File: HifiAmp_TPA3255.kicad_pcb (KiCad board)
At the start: 4 copper layers, 200 x 150 mm, 124 parts, among them J1 PVDD 48V IN — NEEDS_DATA, J2 RCA L SE, J3 RCA R SE, J301 SPK_L, J302 SPK_R, J4 VOLUME_REMOTE, Q301 IPP330P10NM, Q302 IXTK200N10L2, U1 LM5010ASD, U2 LM2940IMP-12/NOPB, U3 TLV1117-33IDCY, U4 OPA1612AIDR, U5 OPA1612AIDR, U6 TPA3255B, U7 TPS3802K33DCKR, U8 LM5069-2

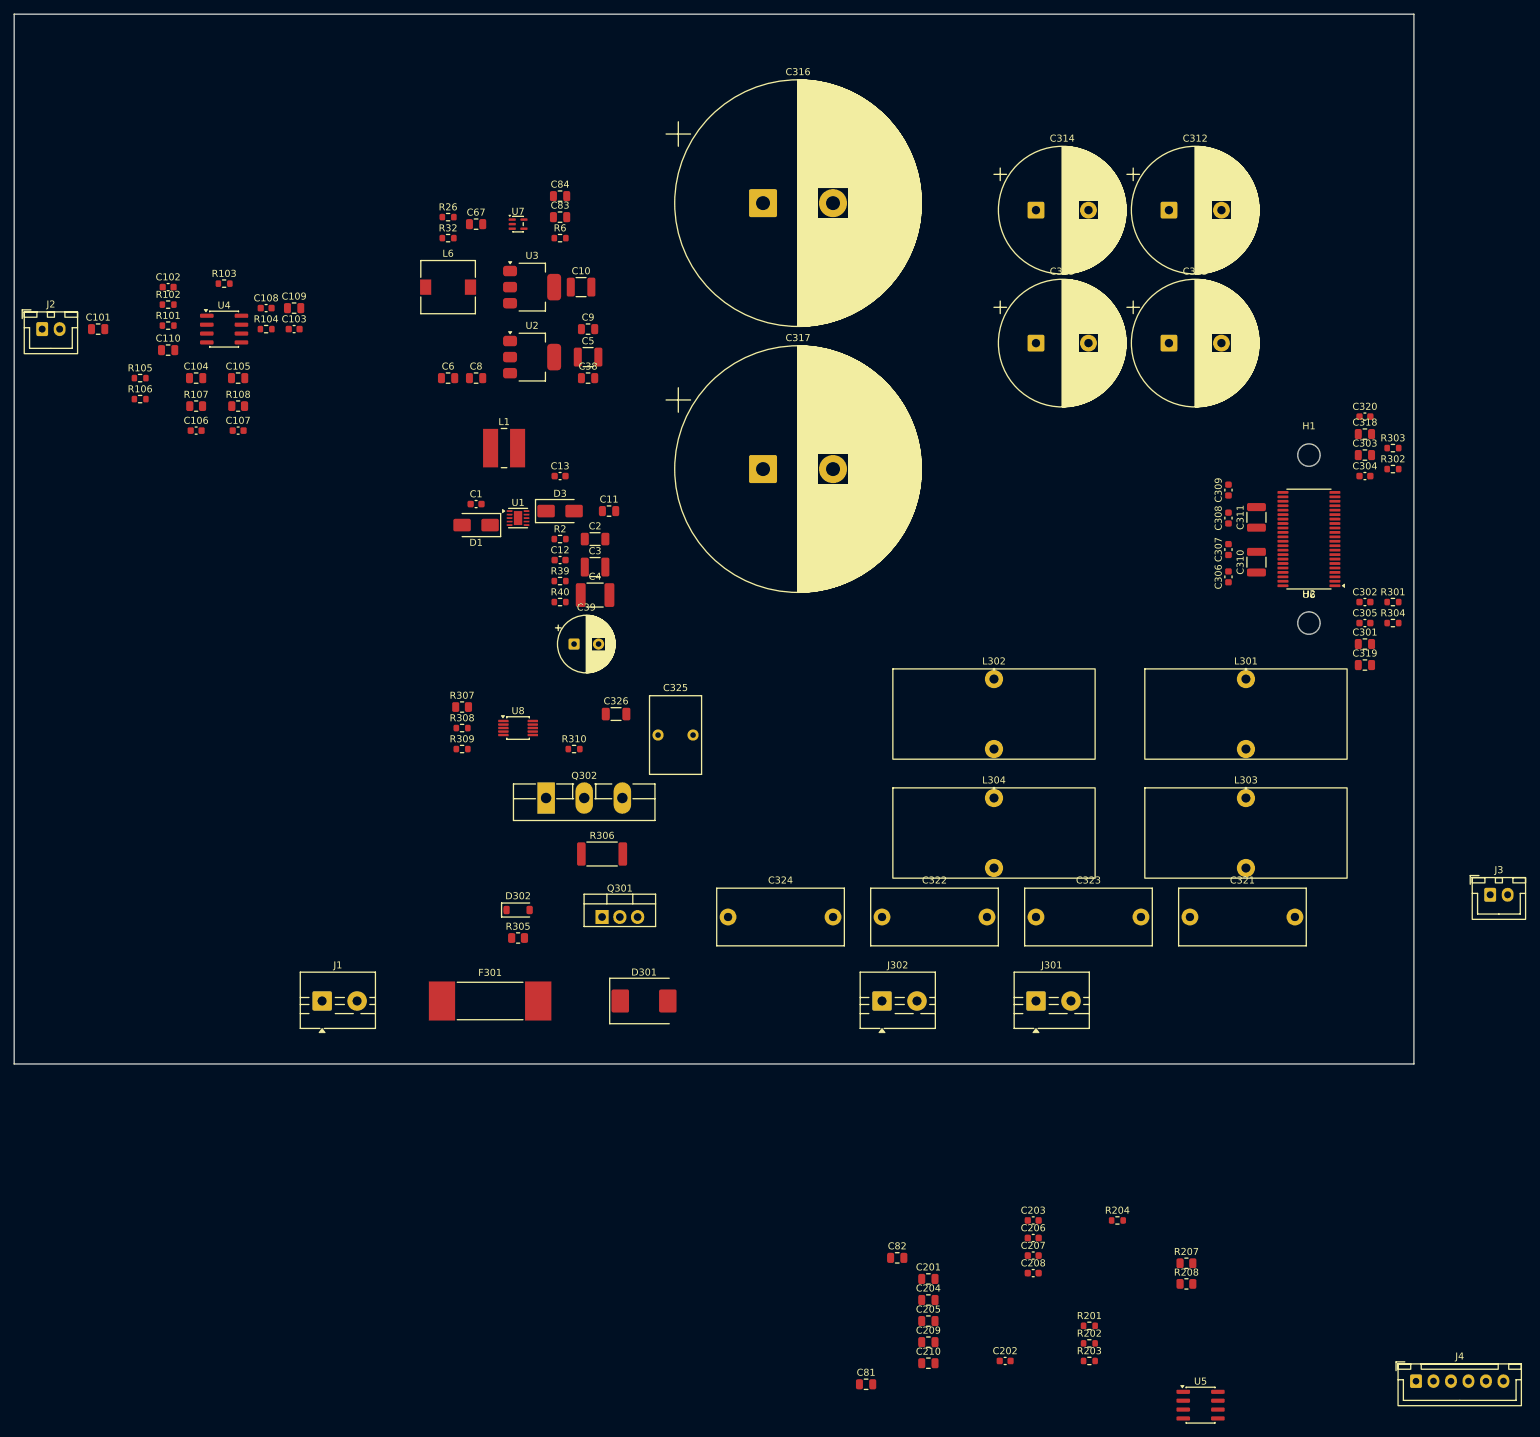
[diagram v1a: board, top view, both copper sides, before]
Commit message: feat(e1.4): mirror the left channel onto the right, and close the placement
The last 21 footprints go down as a pure translation of the left channel,
+40 mm in y and same x: U5 at (130, 185) against U4 at (130, 145), each
series-200 satellite on its series-100 twin's homologue. C210 stays glued to
U5 for the reason C110 stays glued to U4. C81/C82 close the +12V-OA rail
downstream of L6, and J3/J4 leave through the front panel. Nothing crosses
x = 156, where E1.3's auxiliary supply block starts.

The translation is deliberate rather than convenient: it lets E1.5 judge
inter-channel symmetry on measured geometry instead of on stated intent.

The import block is now empty — all 124 footprints are placed.

DRC: 104 violations, all silkscreen (85 silk_overlap, 19 silk_over_copper);
no clearance, no courtyards_overlap, lib_footprint_mismatch still 0;
pad_prop_heatsink still present once, so E1.10's regression did not recur;
schematic_parity 0; 254 unconnected. The diff touches 21 (at ...) lines and
nothing else, which is what proves the 103 earlier placements intact.

Co-Authored-By: Claude Opus 5 <noreply@anthropic.com>
Claude-Session: https://claude.ai/code/session_01JQiSdGemgJKtPWgNcZMmbY
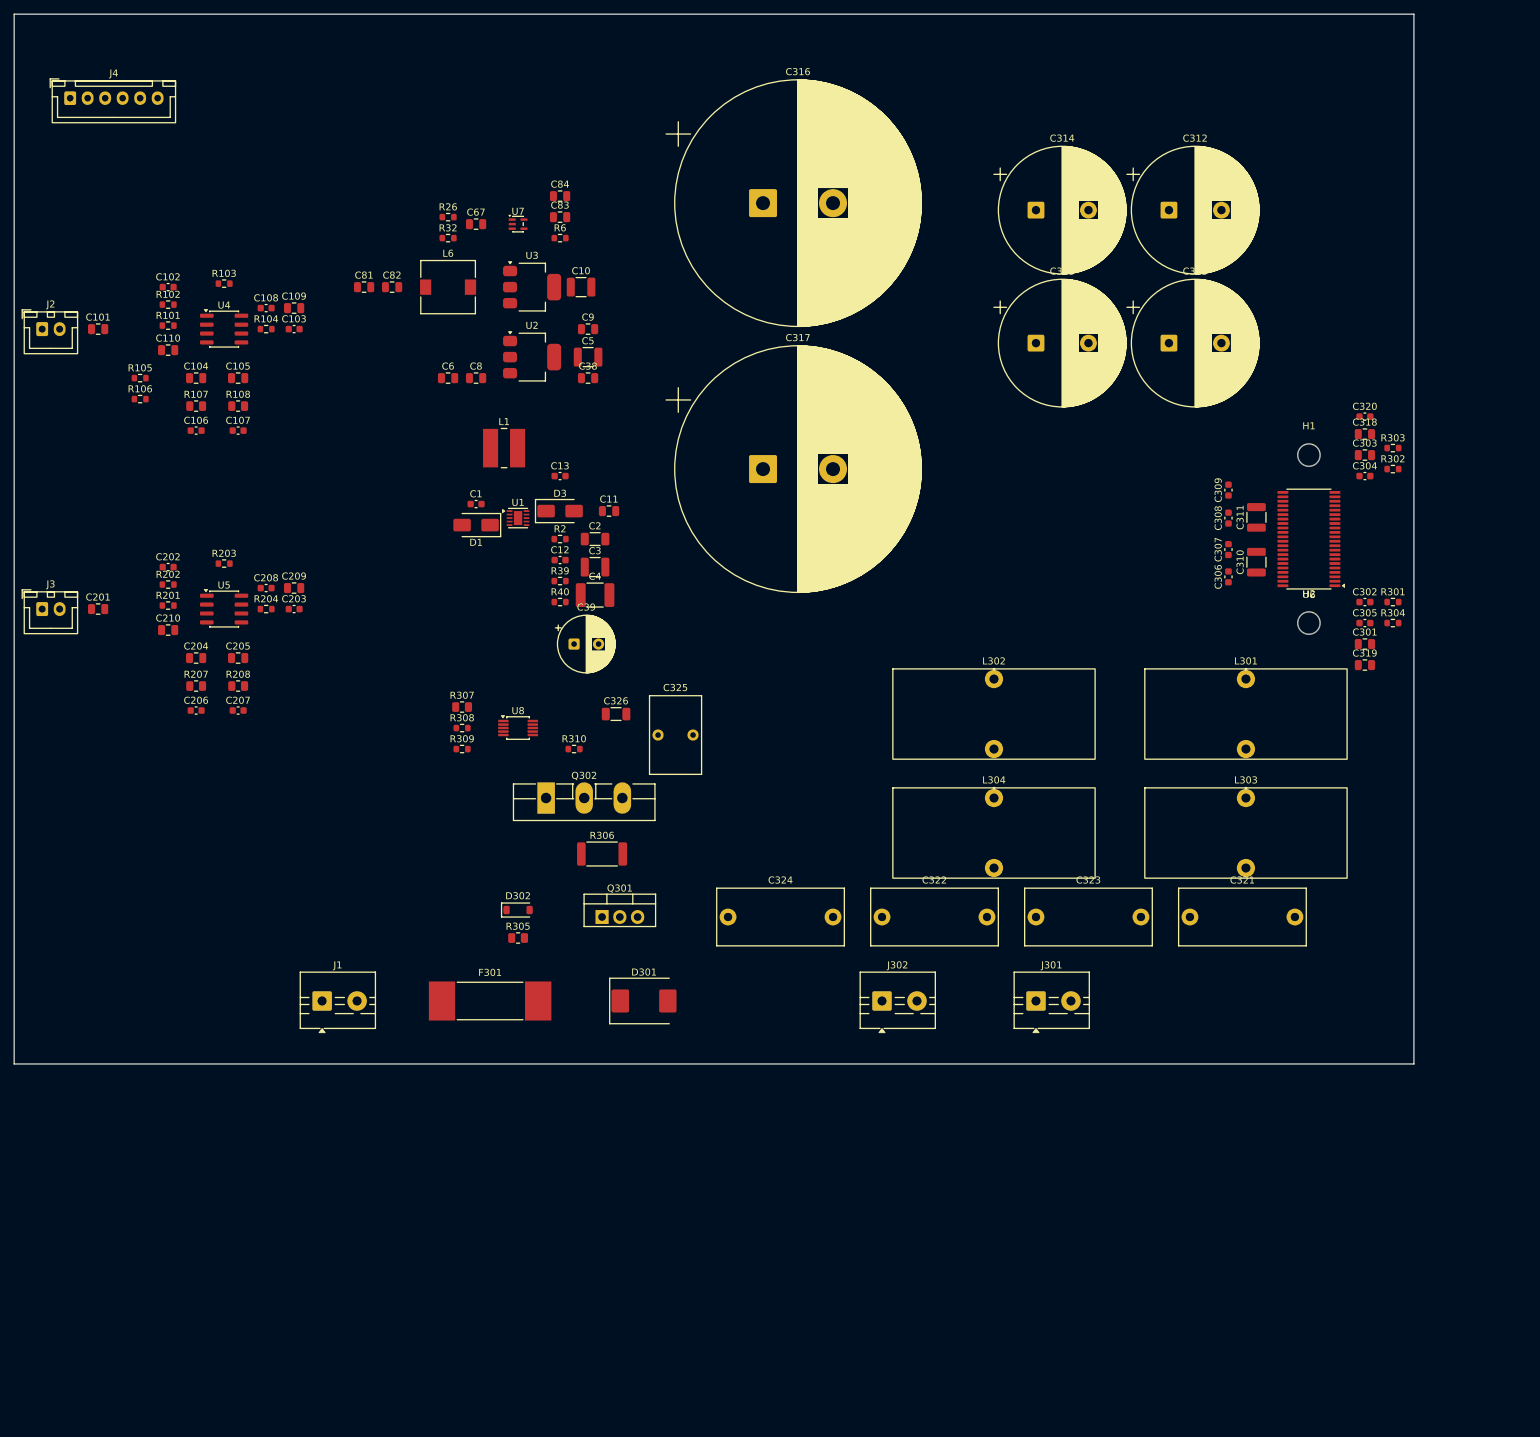
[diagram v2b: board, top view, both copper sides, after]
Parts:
- moved J4 265.7 mm to (108.0, 112.0)
- moved J3 210.9 mm to (104.0, 185.0)
- moved U5 180.0 mm to (130.0, 185.0)
- moved C81 172.4 mm to (150.0, 139.0)
- moved R202 170.5 mm to (122.0, 181.5)
- moved R203 168.1 mm to (130.0, 178.5)
- moved R201 167.1 mm to (122.0, 184.5)
- moved C202 164.8 mm to (122.0, 179.0)
- moved R207 163.8 mm to (126.0, 196.0)
- moved R208 160.2 mm to (132.0, 196.0)
- moved C82 156.4 mm to (154.0, 139.0)
- moved C201 152.4 mm to (112.0, 185.0)
- moved C210 150.9 mm to (122.0, 188.0)
- moved R204 149.8 mm to (136.0, 185.0)
- moved C208 147.0 mm to (136.0, 182.0)
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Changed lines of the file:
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@@
 	(footprint "Resistor_SMD:R_0603_1608Metric"
 		(layer "F.Cu")
-		(at 257.635 272.355)
+		(at 136 185)
 		(descr "Resistor SMD 0603 (1608 Metric), square (rectangular) end terminal, IPC-7351 nominal, (Body size source: IPC-SM-782 page 72, https://www.pcb-3d.com/wordpress/wp-content/uploads/ipc-sm-782a_amendment_1_and_2.pdf)")
 		(tags "resistor")
@@
 	(footprint "Connector_JST:JST_XH_B2B-XH-A_1x02_P2.50mm_Vertical"
 		(layer "F.Cu")
-		(at 310.895 225.825)
+		(at 104 185)
 		(descr "JST XH series connector, B2B-XH-A (http://www.jst-mfg.com/product/pdf/eng/eXH.pdf)")
 		(tags "connector JST XH vertical")
@@
 	(footprint "Capacitor_SMD:C_0805_2012Metric"
 		(layer "F.Cu")
-		(at 230.625 283.725)
+		(at 126 192)
 		(descr "Capacitor SMD 0805 (2012 Metric), square (rectangular) end terminal, IPC-7351 nominal, (Body size source: IPC-SM-782 page 76, https://www.pcb-3d.com/wordpress/wp-content/uploads/ipc-sm-782a_amendment_1_and_2.pdf, https://docs.google.com/spreadsheets/d/1BsfQQcO9C6DZCsRaXUlFlo91Tg2WpOkGARC1WS5S8t0/edit?usp=sharing)")
 		(tags "capacitor")
@@
 	(footprint "Capacitor_SMD:C_0603_1608Metric"
 		(layer "F.Cu")
-		(at 241.595 292.435)
+		(at 122 179)
 		(descr "Capacitor SMD 0603 (1608 Metric), square (rectangular) end terminal, IPC-7351 nominal, (Body size source: IPC-SM-782 page 76, https://www.pcb-3d.com/wordpress/wp-content/uploads/ipc-sm-782a_amendment_1_and_2.pdf)")
 		(tags "capacitor")
@@
 	(footprint "Capacitor_SMD:C_0603_1608Metric"
 		(layer "F.Cu")
-		(at 245.605 274.865)
+		(at 126 199.5)
 		(descr "Capacitor SMD 0603 (1608 Metric), square (rectangular) end terminal, IPC-7351 nominal, (Body size source: IPC-SM-782 page 76, https://www.pcb-3d.com/wordpress/wp-content/uploads/ipc-sm-782a_amendment_1_and_2.pdf)")
 		(tags "capacitor")
@@
 	(footprint "Capacitor_SMD:C_0805_2012Metric"
 		(layer "F.Cu")
-		(at 230.625 289.745)
+		(at 140 182)
 		(descr "Capacitor SMD 0805 (2012 Metric), square (rectangular) end terminal, IPC-7351 nominal, (Body size source: IPC-SM-782 page 76, https://www.pcb-3d.com/wordpress/wp-content/uploads/ipc-sm-782a_amendment_1_and_2.pdf, https://docs.google.com/spreadsheets/d/1BsfQQcO9C6DZCsRaXUlFlo91Tg2WpOkGARC1WS5S8t0/edit?usp=sharing)")
 		(tags "capacitor")
@@
 	(footprint "Capacitor_SMD:C_0603_1608Metric"
 		(layer "F.Cu")
-		(at 245.605 277.375)
+		(at 132 199.5)
 		(descr "Capacitor SMD 0603 (1608 Metric), square (rectangular) end terminal, IPC-7351 nominal, (Body size source: IPC-SM-782 page 76, https://www.pcb-3d.com/wordpress/wp-content/uploads/ipc-sm-782a_amendment_1_and_2.pdf)")
 		(tags "capacitor")
@@
 	(footprint "Package_SO:SOIC-8_3.9x4.9mm_P1.27mm"
 		(layer "F.Cu")
-		(at 269.515 298.745)
+		(at 130 185)
 		(descr "SOIC, 8 Pin (JEDEC MS-012AA, https://www.analog.com/media/en/package-pcb-resources/package/pkg_pdf/soic_narrow-r/r_8.pdf)")
 		(tags "SOIC SO")
@@
 	(footprint "Capacitor_SMD:C_0603_1608Metric"
 		(layer "F.Cu")
-		(at 245.605 272.355)
+		(at 140 185)
 		(descr "Capacitor SMD 0603 (1608 Metric), square (rectangular) end terminal, IPC-7351 nominal, (Body size source: IPC-SM-782 page 76, https://www.pcb-3d.com/wordpress/wp-content/uploads/ipc-sm-782a_amendment_1_and_2.pdf)")
 		(tags "capacitor")
@@
 	(footprint "Resistor_SMD:R_0603_1608Metric"
 		(layer "F.Cu")
-		(at 253.625 289.925)
+		(at 122 181.5)
 		(descr "Resistor SMD 0603 (1608 Metric), square (rectangular) end terminal, IPC-7351 nominal, (Body size source: IPC-SM-782 page 72, https://www.pcb-3d.com/wordpress/wp-content/uploads/ipc-sm-782a_amendment_1_and_2.pdf)")
 		(tags "resistor")
@@
 	(footprint "Capacitor_SMD:C_0805_2012Metric"
 		(layer "F.Cu")
-		(at 230.625 286.735)
+		(at 132 192)
 		(descr "Capacitor SMD 0805 (2012 Metric), square (rectangular) end terminal, IPC-7351 nominal, (Body size source: IPC-SM-782 page 76, https://www.pcb-3d.com/wordpress/wp-content/uploads/ipc-sm-782a_amendment_1_and_2.pdf, https://docs.google.com/spreadsheets/d/1BsfQQcO9C6DZCsRaXUlFlo91Tg2WpOkGARC1WS5S8t0/edit?usp=sharing)")
 		(tags "capacitor")
@@
 	(footprint "Connector_JST:JST_XH_B6B-XH-A_1x06_P2.50mm_Vertical"
 		(layer "F.Cu")
-		(at 300.295 295.315)
+		(at 108 112)
 		(descr "JST XH series connector, B6B-XH-A (http://www.jst-mfg.com/product/pdf/eng/eXH.pdf)")
 		(tags "connector JST XH vertical")
@@
 	(footprint "Resistor_SMD:R_0805_2012Metric"
 		(layer "F.Cu")
-		(at 267.495 278.475)
+		(at 126 196)
 		(descr "Resistor SMD 0805 (2012 Metric), square (rectangular) end terminal, IPC-7351 nominal, (Body size source: IPC-SM-782 page 72, https://www.pcb-3d.com/wordpress/wp-content/uploads/ipc-sm-782a_amendment_1_and_2.pdf)")
 		(tags "resistor")
@@
 	(footprint "Resistor_SMD:R_0603_1608Metric"
 		(layer "F.Cu")
-		(at 253.625 287.415)
+		(at 122 184.5)
 		(descr "Resistor SMD 0603 (1608 Metric), square (rectangular) end terminal, IPC-7351 nominal, (Body size source: IPC-SM-782 page 72, https://www.pcb-3d.com/wordpress/wp-content/uploads/ipc-sm-782a_amendment_1_and_2.pdf)")
 		(tags "resistor")
@@
 	(footprint "Capacitor_SMD:C_0805_2012Metric"
 		(layer "F.Cu")
-		(at 221.725 295.765)
+		(at 150 139)
 		(descr "Capacitor SMD 0805 (2012 Metric), square (rectangular) end terminal, IPC-7351 nominal, (Body size source: IPC-SM-782 page 76, https://www.pcb-3d.com/wordpress/wp-content/uploads/ipc-sm-782a_amendment_1_and_2.pdf, https://docs.google.com/spreadsheets/d/1BsfQQcO9C6DZCsRaXUlFlo91Tg2WpOkGARC1WS5S8t0/edit?usp=sharing)")
 		(tags "capacitor")
@@
 	(footprint "Capacitor_SMD:C_0805_2012Metric"
 		(layer "F.Cu")
-		(at 230.625 292.755)
+		(at 122 188)
 		(descr "Capacitor SMD 0805 (2012 Metric), square (rectangular) end terminal, IPC-7351 nominal, (Body size source: IPC-SM-782 page 76, https://www.pcb-3d.com/wordpress/wp-content/uploads/ipc-sm-782a_amendment_1_and_2.pdf, https://docs.google.com/spreadsheets/d/1BsfQQcO9C6DZCsRaXUlFlo91Tg2WpOkGARC1WS5S8t0/edit?usp=sharing)")
 		(tags "capacitor")
@@
 	(footprint "Capacitor_SMD:C_0805_2012Metric"
 		(layer "F.Cu")
-		(at 230.625 280.715)
+		(at 112 185)
 		(descr "Capacitor SMD 0805 (2012 Metric), square (rectangular) end terminal, IPC-7351 nominal, (Body size source: IPC-SM-782 page 76, https://www.pcb-3d.com/wordpress/wp-content/uploads/ipc-sm-782a_amendment_1_and_2.pdf, https://docs.google.com/spreadsheets/d/1BsfQQcO9C6DZCsRaXUlFlo91Tg2WpOkGARC1WS5S8t0/edit?usp=sharing)")
 		(tags "capacitor")
@@
 	(footprint "Capacitor_SMD:C_0805_2012Metric"
 		(layer "F.Cu")
-		(at 226.175 277.705)
+		(at 154 139)
 		(descr "Capacitor SMD 0805 (2012 Metric), square (rectangular) end terminal, IPC-7351 nominal, (Body size source: IPC-SM-782 page 76, https://www.pcb-3d.com/wordpress/wp-content/uploads/ipc-sm-782a_amendment_1_and_2.pdf, https://docs.google.com/spreadsheets/d/1BsfQQcO9C6DZCsRaXUlFlo91Tg2WpOkGARC1WS5S8t0/edit?usp=sharing)")
 		(tags "capacitor")
@@
 	(footprint "Capacitor_SMD:C_0603_1608Metric"
 		(layer "F.Cu")
-		(at 245.605 279.885)
+		(at 136 182)
 		(descr "Capacitor SMD 0603 (1608 Metric), square (rectangular) end terminal, IPC-7351 nominal, (Body size source: IPC-SM-782 page 76, https://www.pcb-3d.com/wordpress/wp-content/uploads/ipc-sm-782a_amendment_1_and_2.pdf)")
 		(tags "capacitor")
@@
 	(footprint "Resistor_SMD:R_0805_2012Metric"
 		(layer "F.Cu")
-		(at 267.495 281.425)
+		(at 132 196)
 		(descr "Resistor SMD 0805 (2012 Metric), square (rectangular) end terminal, IPC-7351 nominal, (Body size source: IPC-SM-782 page 72, https://www.pcb-3d.com/wordpress/wp-content/uploads/ipc-sm-782a_amendment_1_and_2.pdf)")
 		(tags "resistor")
@@
 	(footprint "Resistor_SMD:R_0603_1608Metric"
 		(layer "F.Cu")
-		(at 253.625 292.435)
+		(at 130 178.5)
 		(descr "Resistor SMD 0603 (1608 Metric), square (rectangular) end terminal, IPC-7351 nominal, (Body size source: IPC-SM-782 page 72, https://www.pcb-3d.com/wordpress/wp-content/uploads/ipc-sm-782a_amendment_1_and_2.pdf)")
 		(tags "resistor")
